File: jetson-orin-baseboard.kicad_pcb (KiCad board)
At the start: 8 copper layers, 110 x 55 mm, 501 parts, among them IC601 ACPL-217-500E, IC901 TPS7A0518PDBVT, J1 ERF8-040-05.0-L-DV-K-TR, J301 1-2199230-6, J302 2199230-6, J401 USB4105-GF-A, J402 WE_632723300011_alt_symbol, J501 WE_632723300011_alt_symbol, J601 5-2337992-8, J701 WE_68715014522, J702 WE_68715014522, J801 TC2050-IDC-NL, J803 533980471, M1 M2_4222, M301 M2_2280, Q401 BSS138W-7-F, Q402 BSS138W-7-F, Q501 BSS138W-7-F, Q701 BSS138W-7-F, Q702 BSS138W-7-F, Q703 BSS138W-7-F, Q704 BSS138W-7-F, Q801 BSS138W-7-F, Q802 BSS138W-7-F, Q803 BSS138W-7-F, Q804 BSS138W-7-F, Q901 BSS138W-7-F, Q902 BSS138W-7-F, Q903 BSS138W-7-F, SW901 PCM12SMTR, U1 TPD6F003, U201 74LVC2G17GV, U301 74LVC2G07GV, U302 74LVC2G07GV, U401 RB521S30T1G, U402 TPS65988, U403 W25Q80DVUXIE_TR, U405 FT230XQ-R, U406 TPS7B8133DRVR, U407 TUSB1046-DCI, U408 TPD4E05U06QDQARQ1, U409 TPD4E05U06QDQARQ1, U410 TPD4E05U06QDQARQ1, U411 TPD4E05U06QDQARQ1, U412 TPD4E05U06QDQARQ1, U501 HD3SS3220, U503 AP22615, U505 TPD4E05U06QDQARQ1, U507 TPD4E05U06QDQARQ1, U509 TPD4E05U06QDQARQ1, U601 TPS2372-3RGWR, U602 ULS-12/5-D48N-C, U701 PCA9547BS, U702 AP22615, U703 AP22615, U704 NX3DV642, U705 NX3DV642, U706 AP22615, U707 AP22615, U803 PCAL6416AHF, U805 AP22615, U806 AP22615, U807 74LVC1T45GM, U901 RB521S30T1G, U902 RB521S30T1G, U903 MP2386GG-P, U904 MP2386GG-P, U905 74LVC2G14GV, U906 74LVC1G175GV

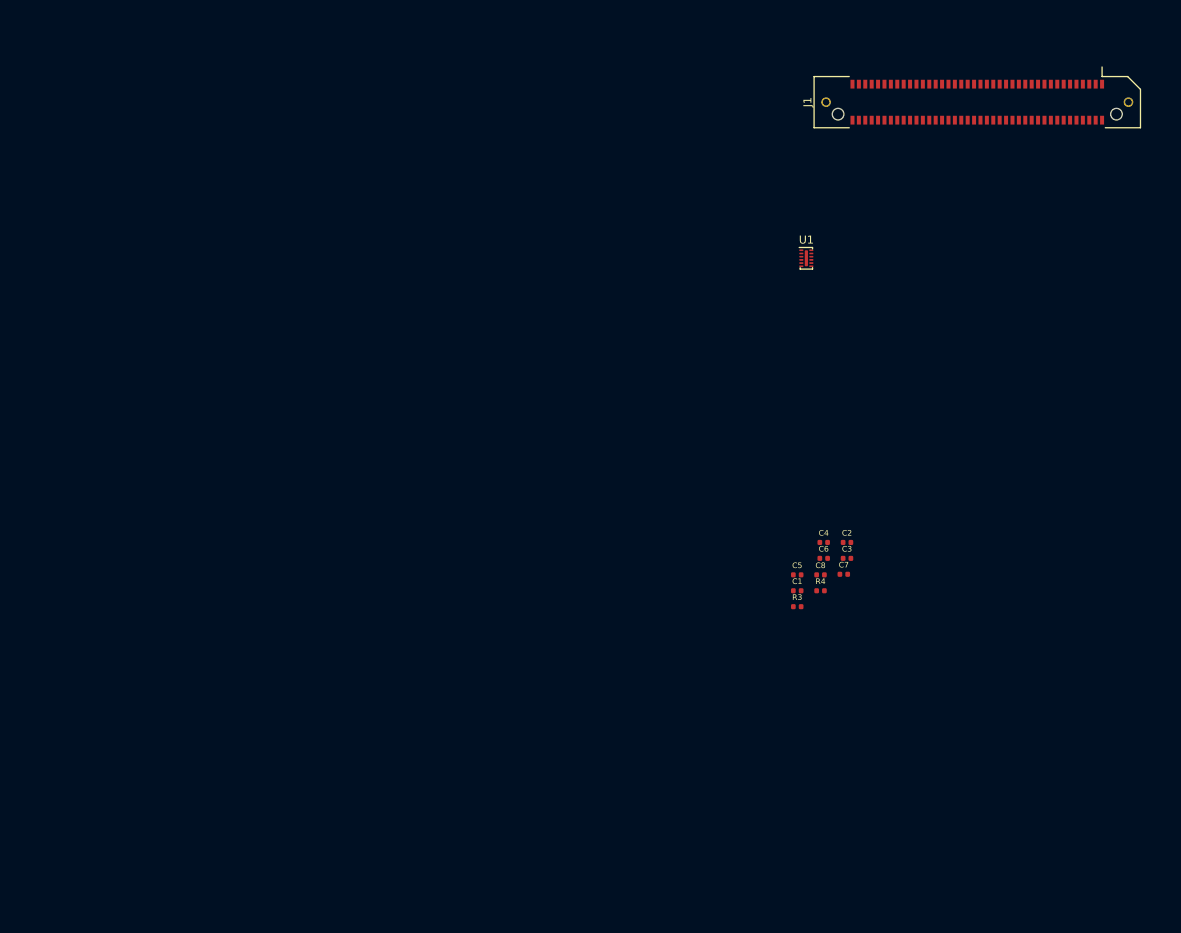
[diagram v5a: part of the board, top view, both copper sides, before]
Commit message: Add Jetson Orin NX/Nano 3D model
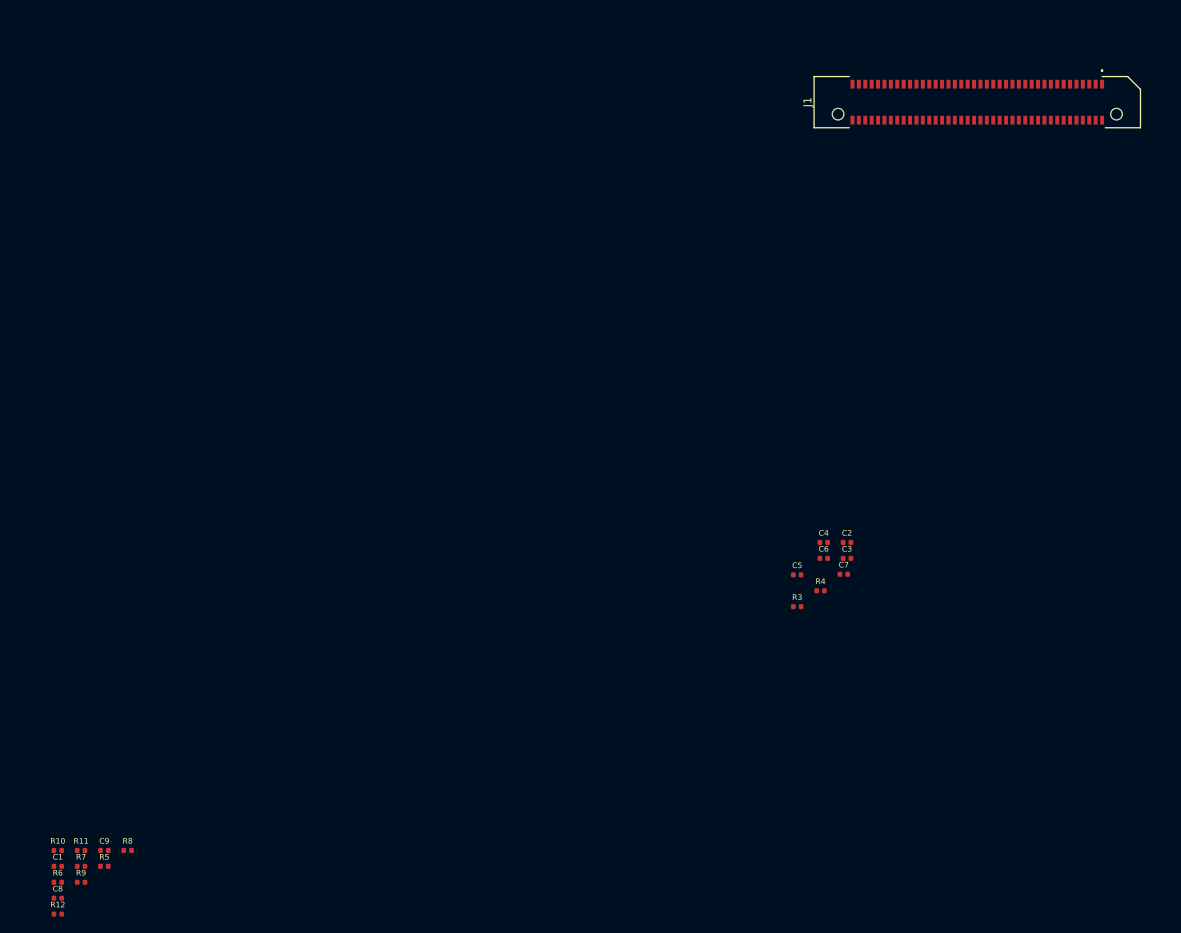
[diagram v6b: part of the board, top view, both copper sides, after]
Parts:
- removed U1: TPD6F003, Package_SON:Texas_R-PWSON-N12_EP0.4x2mm
- added C9: C_1u_0402, antmicro-footprints:0402-cap, F.Cu at (-44.8, 262.5)
- added M2: jetson-orin-nx/nano-module, antmicro-footprints:jetson-orin-nx-nano-module, F.Cu at (124.8, 119.4)
- added R10: R_0R_0402, antmicro-footprints:0402-res, F.Cu at (-50.6, 262.5)
- added R11: R_0R_0402, antmicro-footprints:0402-res, F.Cu at (-47.7, 262.5)
- added R12: R_0R_0402, antmicro-footprints:0402-res, F.Cu at (-50.6, 270.5)
- added R5: R_0R_0402, antmicro-footprints:0402-res, F.Cu at (-44.8, 264.5)
- added R6: R_0R_0402, antmicro-footprints:0402-res, F.Cu at (-50.6, 266.5)
- added R7: R_0R_0402, antmicro-footprints:0402-res, F.Cu at (-47.7, 264.5)
- added R8: R_0R_0402, antmicro-footprints:0402-res, F.Cu at (-41.8, 262.5)
- added R9: R_0R_0402, antmicro-footprints:0402-res, F.Cu at (-47.7, 266.5)
- C1, C8: value C_100n_0402 -> C_1u_0402
- J1: footprint antmicro-footprints:ERF8-XXX-XX.X-X-DV-XXXX-TR -> antmicro-footprints:ERF8-040-XX.X-X-DV-XX
- moved C8 103.6 mm to (-50.6, 268.5)
- moved C1 98.6 mm to (-50.6, 264.5)
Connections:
- net Net-(C2-Pad2) renamed /Peripherals/PCIE2_TX0_CONN_N
- net Net-(C3-Pad2) renamed /Peripherals/PCIE2_TX0_CONN_P
- net Net-(C4-Pad2) renamed /Peripherals/PCIE2_TX1_CONN_P
- net Net-(C5-Pad2) renamed /Peripherals/USBSS2_TX_CONN_P
- net Net-(C6-Pad2) renamed /Peripherals/PCIE2_TX1_CONN_N
- net Net-(C7-Pad2) renamed /Peripherals/USBSS2_TX_CONN_N
- net Net-(J1-Pad21) renamed /Peripherals/USBSS2_RX_CONN_N
- net Net-(J1-Pad23) renamed /Peripherals/USBSS2_RX_CONN_P
- C8 pad 1: /Peripherals/CONN_3V3 -> 3V3_STDB
- J1 pad 15: PCIE2_CLK_N -> /Peripherals/PCIE2_CLK_CONN_N
- J1 pad 17: PCIE2_CLK_P -> /Peripherals/PCIE2_CLK_CONN_P
- J1 pad 18: PCIE3_CLK_N -> /Peripherals/PCIE3_CLK_CONN_N
- J1 pad 20: PCIE3_CLK_P -> /Peripherals/PCIE3_CLK_CONN_P
- J1 pad 27: /Peripherals/EXT_GPIO2 -> PCIE2_RST*
- J1 pad 29: /Peripherals/EXT_GPIO3 -> PCIE2_CLKREQ*
- J1 pad 3: PCIE2_RX0_N -> /Peripherals/PCIE2_RX0_CONN_N
- J1 pad 30: /Peripherals/EXT_GPIO0 -> PCIE3_RST*
- J1 pad 32: /Peripherals/EXT_GPIO1 -> PCIE3_CLKREQ*
- J1 pad 33: GPIO12 -> /Peripherals/EXT_GPIO2
- J1 pad 35: GPIO13 -> /Peripherals/EXT_GPIO3
- J1 pad 36: GPIO01 -> /Peripherals/EXT_GPIO0
- J1 pad 38: GPIO07 -> /Peripherals/EXT_GPIO1
- J1 pad 39: PCIE2_RST* -> GPIO12
- J1 pad 41: PCIE2_CLKREQ* -> GPIO13
- J1 pad 42: PCIE3_RST* -> GPIO01
- J1 pad 44: PCIE3_CLKREQ* -> GPIO07
- J1 pad 5: PCIE2_RX0_P -> /Peripherals/PCIE2_RX0_CONN_P
- J1 pad 6: PCIE2_RX1_N -> /Peripherals/PCIE2_RX1_CONN_N
- J1 pad 8: PCIE2_RX1_P -> /Peripherals/PCIE2_RX1_CONN_P

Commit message: Import changes to PCB, place part of components inside PCB, temporarily remove part of components on PCB
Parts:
- removed C1, C8, C9, C910, C927: C_1u_0402, antmicro-footprints:0402-cap
- removed C2, C205, C3, C305, C306, C307, C308, C309, C310, C311, C312, C313, C318, C4, C401, C412, C415, C421, C422, C425, C427, C429, C431, C432, C440, C442, C5, C503, C505, C507, C508, C511, C512, C515, C519, C6, C607, C611, C7, C804, C808, C809, C810, C812, C922: C_100n_0402, antmicro-footprints:0402-cap
- removed C201, C202, C203, C204, C901, C902, C905, C906, C907: C_22u_0805_25V, antmicro-footprints:0805-cap
- removed C301, C302, C303, C304, C323, C324, C501, C517: C_10u_0603, antmicro-footprints:0603-cap
- removed C434: C_10u_25V_0603, antmicro-footprints:0603-cap
- removed C436, C912: C_10u_0402, antmicro-footprints:0402-cap
- removed C601: C_100n_0805_100V, antmicro-footprints:0805-cap
- removed C602: C_10n_0402, antmicro-footprints:0402-cap
- removed C604: C_22u_2220_100V, antmicro-footprints:2220-cap
- removed C608, C609: C_47u_16V_1206, antmicro-footprints:1206-cap
- removed C610: C_100n_0402_16V, antmicro-footprints:0402-cap
- removed C908: C_100n_0402_50V, antmicro-footprints:0402-cap
- removed C914: C_220n_0402, antmicro-footprints:0402-cap
- removed C916: C_33p_0402, antmicro-footprints:0402-cap
- removed C918, C923: C_22u_0402, antmicro-footprints:0402-cap
- removed D301, D604: KP-1608CGCK, antmicro-footprints:LED_0603
- removed D402, D405, D408, D503, D801, D802, D803: LTST-C190GKT, antmicro-footprints:LED_0603
- removed D501: ESD9X5.0ST5G, antmicro-footprints:SOD-923
- removed D601, D602: CD-MMBL110S, antmicro-footprints:DFN3538
- removed D603: PTVS58VS1UR,115, antmicro-footprints:SOD-123F
- removed D605: PDS760-13, antmicro-footprints:PDS760-13
- removed FB201: 74279221100, antmicro-footprints:1206-res
- removed FB601, FB602: BLM21PG221SN1D, antmicro-footprints:0805-res
- removed IC601: ACPL-217-500E, antmicro-footprints:SOIC127P700X242-4N
- removed IC901: TPS7A0518PDBVT, antmicro-footprints:SOT-23-5
- removed J803: 533980471, antmicro-footprints:Molex_PicoBlade_53398-0471_1x04-1MP_P1.25mm_Vertical
- removed Q501, Q801, Q803, Q804, Q902, Q903: BSS138W-7-F, antmicro-footprints:SOT-323
- removed R1, R10, R11, R12, R2, R201, R202, R203, R205, R206, R207, R208, R209, R210, R211, R212, R3, R304, R305, R306, R308, R309, R316, R4, R401, R407, R408, R410, R420, R424, R425, R429, R430, R431, R433, R434, R453, R456, R458, R5, R503, R504, R510, R511, R512, R513, R514, R515, R516, R517, R532, R533, R534, R535, R536, R537, R6, R7, R8, R802, R803, R804, R806, R811, R812, R813, R814, R815, R816, R817, R9, R905, R914, R916: R_0R_0402, antmicro-footprints:0402-res
- removed R204, R301, R302, R303, R312, R313, R402, R505, R507, R509, R529, R545, R547, R549, R551, R608, R609, R612, R821, R822, R823, R826, R827, R828: R_10k_0402, antmicro-footprints:0402-res
- removed R307: R_330R_0603, antmicro-footprints:0603-res
- removed R403, R435, R808, R818, R820, R907: R_100k_0402, antmicro-footprints:0402-res
- removed R423, R427, R829: R_200R_0603, antmicro-footprints:0603-res
- removed R436, R437, R438, R440, R441, R442, R444, R445, R447, R449, R902: R_1k_0402, antmicro-footprints:0402-res
- removed R459, R460: R_2M0_0402, antmicro-footprints:0402-res
- removed R527, R906: R_200k_0402, antmicro-footprints:0402-res
- removed R531: R_887k_0402, antmicro-footprints:0402-res
- removed R553: R_2k2_0402, antmicro-footprints:0402-res
- removed R555: R_470R_0603, antmicro-footprints:0603-res
- removed R601: R_1k3_0603, antmicro-footprints:0603-res
- removed R602: R_49k9_0402, antmicro-footprints:0402-res
- removed R603, R607, R616: R_0R_0603, antmicro-footprints:0603-res
- removed R604: R_63R4_0603, antmicro-footprints:0603-res
- removed R605: R_1k2_0402, antmicro-footprints:0402-res
- removed R606: R_24k9_0402, antmicro-footprints:0402-res
- removed R610, R611: R_220R_0402, antmicro-footprints:0402-res
- removed R613: R_32k4_0402, antmicro-footprints:0402-res
- removed R614, R615: R_1k_0603, antmicro-footprints:0603-res
- removed R617, R819: R_200R_0402, antmicro-footprints:0402-res
- removed R807: R_10k2_0402, antmicro-footprints:0402-res
- removed R824, R825: R_4k7_0402, antmicro-footprints:0402-res
- removed R911: R_40k2_1%_0402, antmicro-footprints:0402-res
- removed S901, S902: B3U-3000PM, antmicro-footprints:B3U-3000P
- removed TP201, TP202, TP403, TP405, TP406, TP408, TP409, TP411, TP412, TP413, TP501, TP505, TP506, TP507, TP801, TP802, TP901, TP903, TP905, TP906: TP_SMD_0_75MM, antmicro-footprints:Testpoint_smd_0_75mm
- removed U201: 74LVC2G17GV, antmicro-footprints:SC-74
- removed U301, U302: 74LVC2G07GV, antmicro-footprints:SC-74
- removed U408, U409, U411, U505, U507, U509: TPD4E05U06QDQARQ1, antmicro-footprints:TPD4E05U06QDQARQ1
- removed U503, U805, U806: AP22615, antmicro-footprints:TSOT23-6
- removed U601: TPS2372-3RGWR, antmicro-footprints:Texas_RGW0020B
- removed U807: 74LVC1T45GM, antmicro-footprints:SOT-886
- removed U905: 74LVC2G14GV, antmicro-footprints:SOT23-6L
- removed U906: 74LVC1G175GV, antmicro-footprints:SOT-23-6
- added J2: 46756-1001, antmicro-footprints:HDMI_Micro-D_Molex_46765-1x01, F.Cu at (94.2, 123.3)
- added SP6: 9774060151, antmicro-footprints:9774060151, F.Cu at (61.2, 119.3)
- added SP7: 9774060151, antmicro-footprints:9774060151, F.Cu at (124.8, 119.4)
- C603, C605, C606, C701, C702, C703, C704, C705, C706, C707, C708, C709, C710, C711, D701, D702, D703, D704, D705, D706, D707, D708, D709, D710, J801, Q701, Q702, Q703, Q704, Q802, R701, R702, R703, R704, R705, R706, R707, R708, R709, R710, R711, R712, R713, R714, R715, R716, R717, R718, R719, R720, R721, R722, R723, R724, R725, R726, R727, R728, R729, R730, R731, R732, R733, R734, R735, R736, R737, R738, R739, R740, R741, R742, R743, R744, R745, R746, R747, R748, R749, R750, R751, R752, R809, S201, S801, S802, SW901, TP702, TP703, TP704, U701, U702, U703, U704, U705, U706, U707, U803: moved to B.Cu
- moved S201 365.2 mm to (118.0, 123.8), turned to 180 degrees
- moved J801 355.7 mm to (130.4, 75.3), turned to 90 degrees
- moved Q802 353.1 mm to (118.8, 73.3), turned to -90 degrees
- moved U803 345.1 mm to (113.5, 74.5), turned to -90 degrees
- moved S802 340.0 mm to (130.7, 123.8), turned to 180 degrees
- moved R809 336.6 mm to (111.3, 79.1), turned to -90 degrees
- moved S801 320.7 mm to (124.3, 123.8), turned to 180 degrees
- moved BAT201 315.3 mm to (75.0, 84.8), turned to 180 degrees
- moved R717 256.3 mm to (113.3, 103.8), turned to 180 degrees
- moved R738 256.3 mm to (113.3, 105.8), turned to 180 degrees
- moved R747 255.7 mm to (113.0, 101.5), turned to 180 degrees
- moved D705 255.4 mm to (112.8, 96.6), turned to 180 degrees
- moved D706 255.4 mm to (112.8, 99.1), turned to 180 degrees
- moved Q701 255.2 mm to (112.7, 93.3), turned to 180 degrees
- moved U707 254.5 mm to (112.4, 88.8), turned to 180 degrees
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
